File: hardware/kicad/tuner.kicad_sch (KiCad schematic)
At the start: 61 parts, among them J1 12V_IN, J2 RADIO_UNIVERSAL, J3 RF_IN_SO239, J4 RF_OUT_SO239, J5 EXT_SWR, J6 ANT_CTRL, J8 DEBUG_UART, Q1 MMBT3904, Q2 MMBT3904, SW1 TUNE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

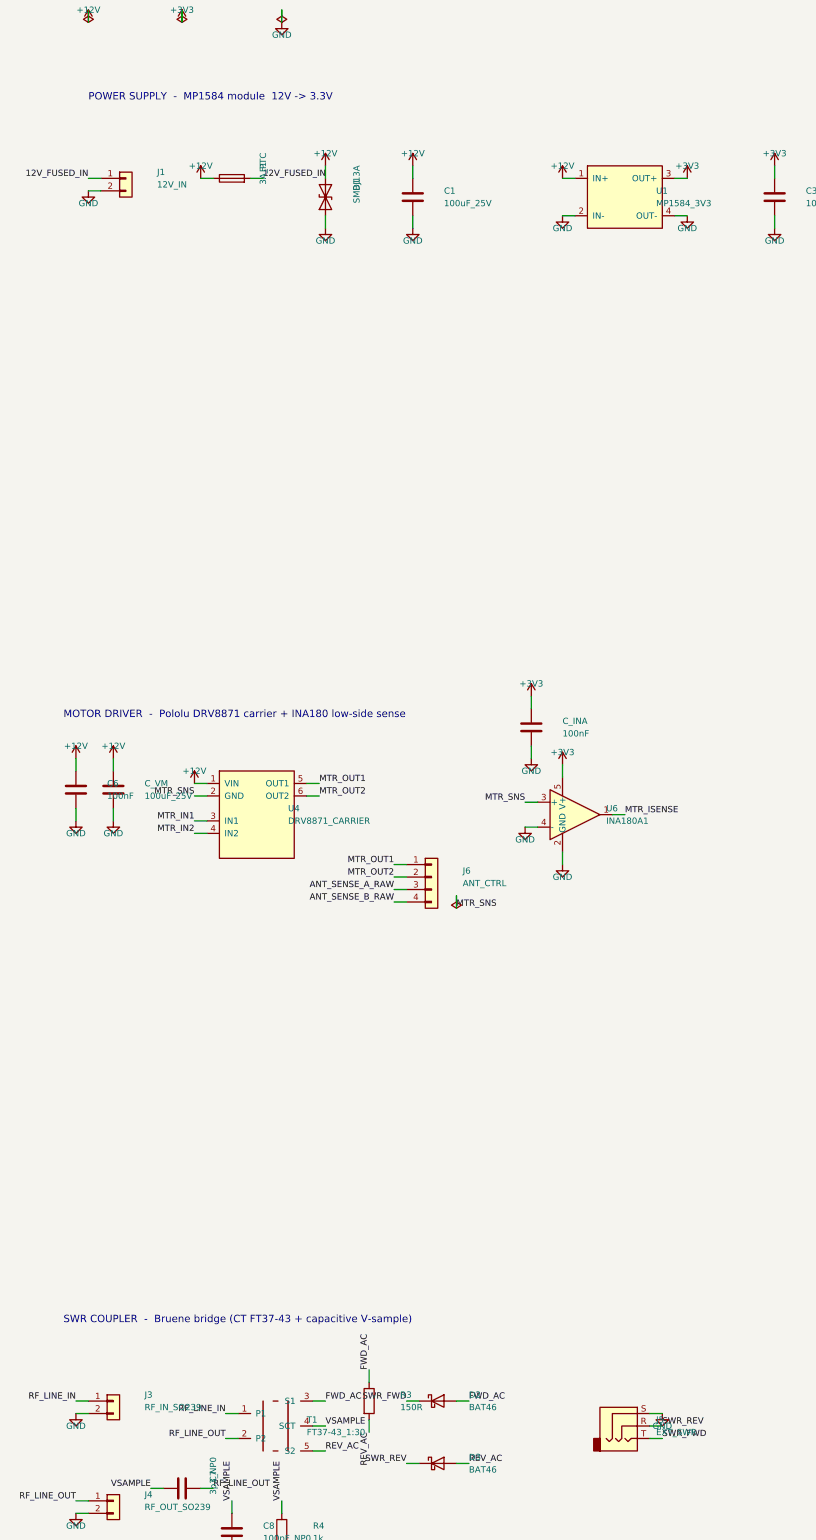
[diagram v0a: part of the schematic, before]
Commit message: Revise power stage and refresh hardware artifacts
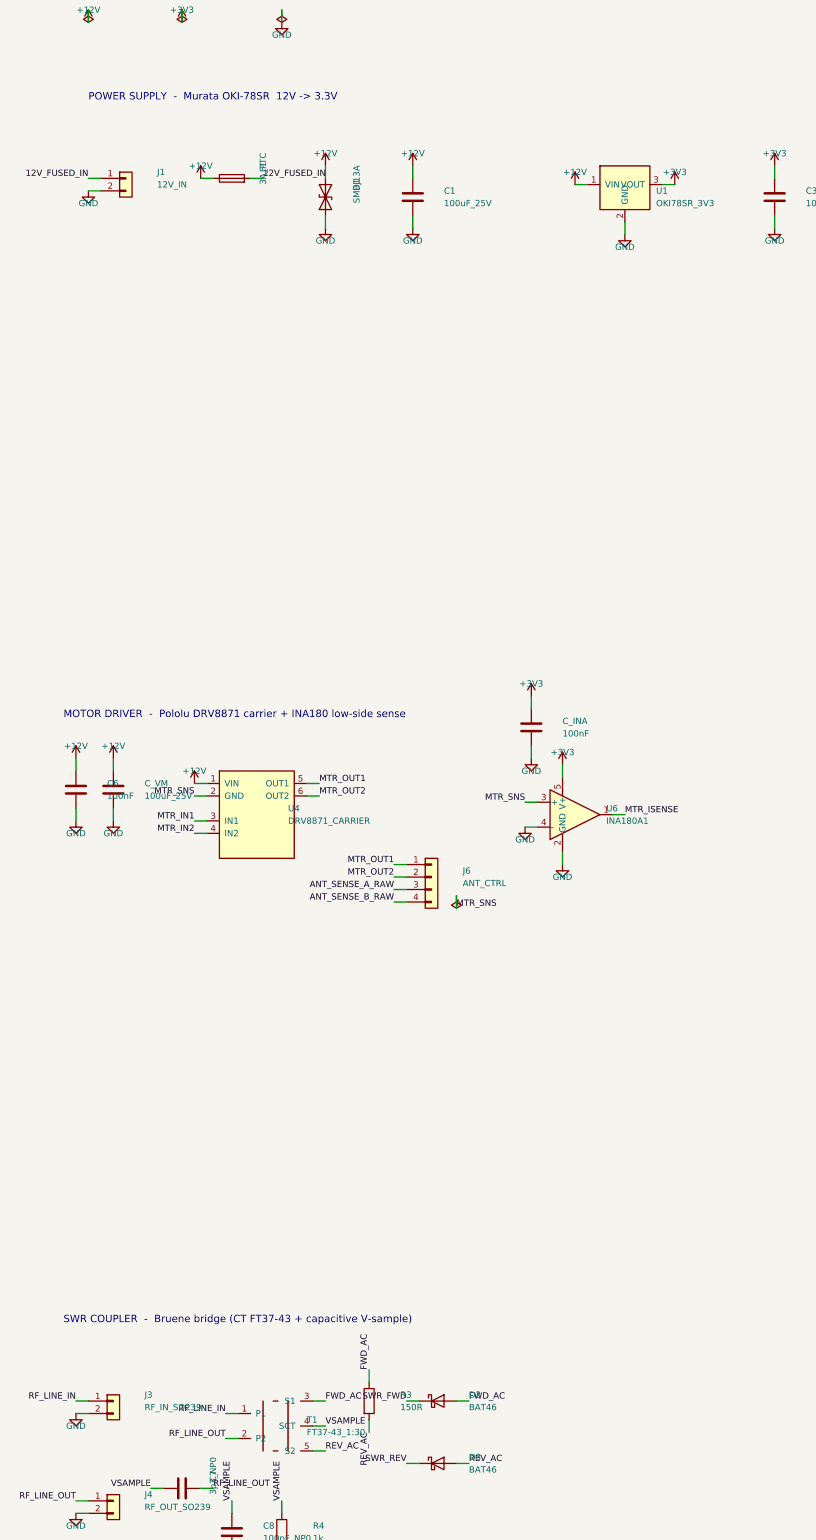
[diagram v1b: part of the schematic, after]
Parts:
- removed J5: EXT_SWR, Connector_Audio:Jack_3.5mm_CUI_SJ1-3533NG_Horizontal, symbol Connector_Audio:AudioJack3
- removed SW1: TUNE, Connector_PinHeader_2.54mm:PinHeader_1x02_P2.54mm_Vertical, symbol Connector_Generic:Conn_01x02
- added J_OLED: SSD1306, Connector_PinHeader_2.54mm:PinHeader_1x04_P2.54mm_Vertical, symbol Connector_Generic:Conn_01x04
- SW1: renamed from J_OLED; value SSD1306 -> TUNE; footprint Connector_PinHeader_2.54mm:PinHeader_1x04_P2.54mm_Vertical -> Connector_PinHeader_2.54mm:PinHeader_1x02_P2.54mm_Vertical; symbol Connector_Generic:Conn_01x04 -> Connector_Generic:Conn_01x02
- U1: value MP1584_3V3 -> OKI78SR_3V3; footprint Tuner:BUCK_MP1584 -> Tuner:REG_OKI78SR; symbol Tuner:BUCK_MP1584 -> Tuner:REG_OKI78SR; MPN (none) -> OKI-78SR-3.3/1.5-W36-C
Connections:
- net +3V3: now also J_OLED.2 (Pin_2); no longer SW1.2 (Pin_2)
- net BTN_TUNE: now also SW1.1 (Pin_1)
- net GND: now also SW1.2 (Pin_2), J_OLED.1 (Pin_1); no longer SW1.1 (Pin_1), U1.4 (OUT-)
- net I2C_SCL: now also J_OLED.3 (Pin_3); no longer SW1.3 (Pin_3)
- net I2C_SDA: now also J_OLED.4 (Pin_4); no longer SW1.4 (Pin_4)
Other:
- note added: "POWER SUPPLY - Murata OKI-78SR 12V -> 3.3V"
- note removed: "POWER SUPPLY - MP1584 module 12V -> 3.3V"
